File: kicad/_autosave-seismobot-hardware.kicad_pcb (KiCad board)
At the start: 4 copper layers, 110 x 111 mm, 98 parts, among them J1 Screw_Terminal_01x02, J2 Raspberry_Pi_2_3, U1 OPA2156xD, U10 AP7340, U2 OPA2156xD, U3 ref-6, U4 ref-8, U5 LTC6011, U6 OPA2156xD, U7 OPA2156xD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

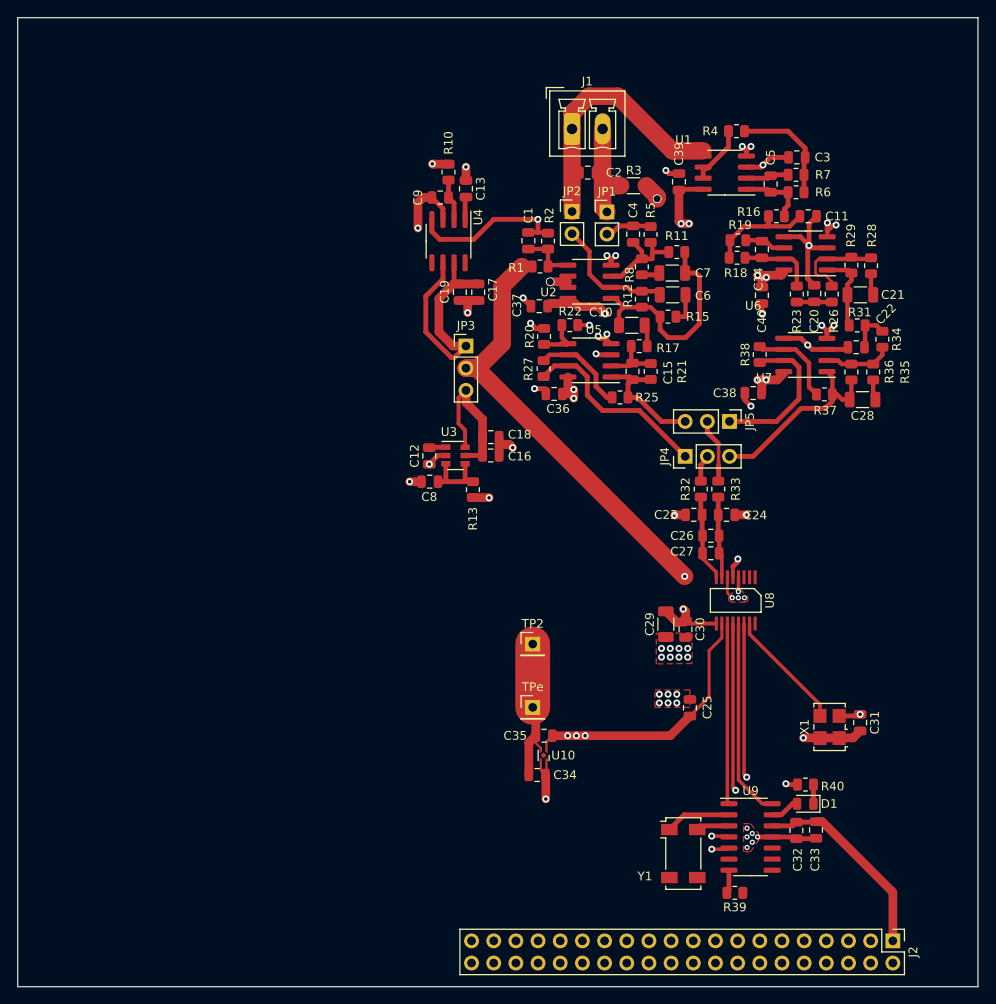
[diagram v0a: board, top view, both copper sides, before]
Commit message: add 3v3 regulator, more routing
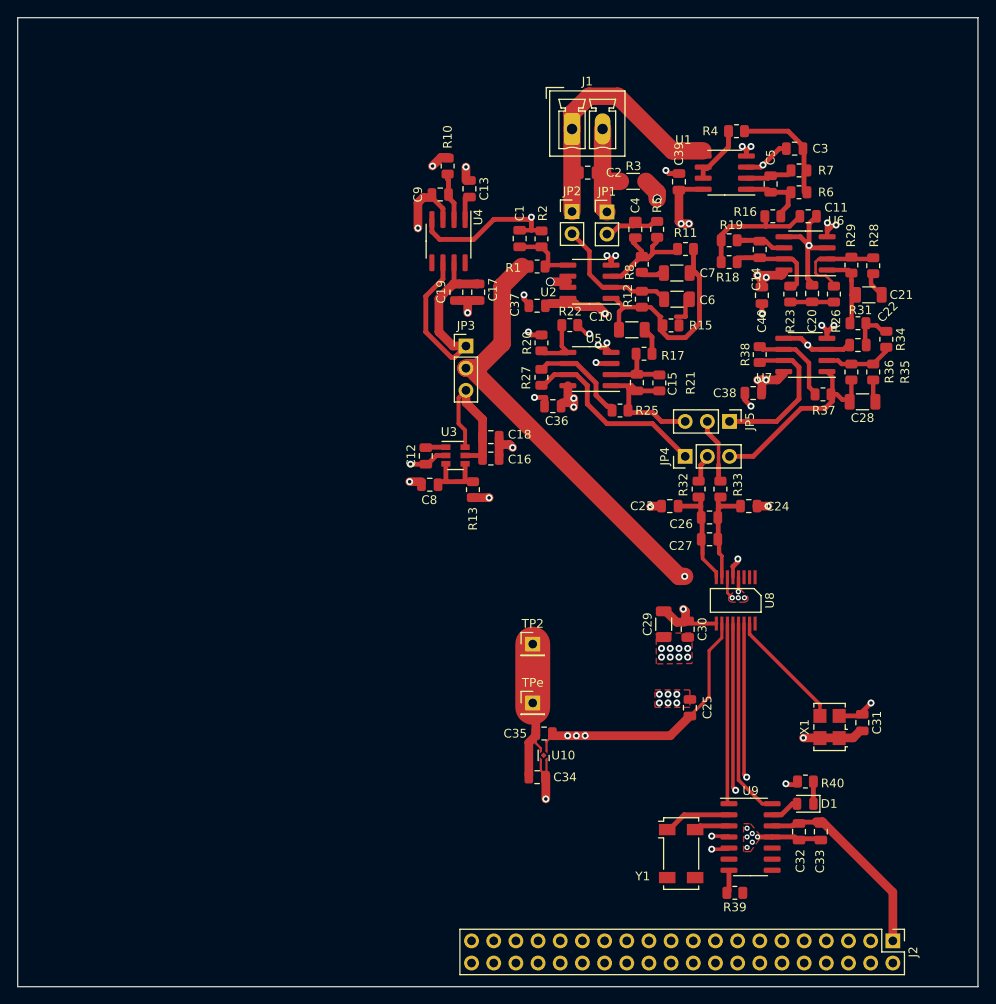
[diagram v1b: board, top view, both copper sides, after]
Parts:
- moved C23 2.93 mm to (133.7, 139.9)
- moved C24 2.74 mm to (142.8, 139.9)
- moved C26 2.11 mm to (138.2, 141.2)
- moved R21 1.64 mm to (132.5, 125.8)
- moved C27 1.61 mm to (138.2, 143.8)
- moved R25 1.50 mm to (128.0, 129.0)
- moved C36 1.41 mm to (120.3, 128.5)
- moved C15 1.38 mm to (129.9, 125.8)
- moved R11 1.06 mm to (135.5, 110.5)
- moved R15 1.06 mm to (133.8, 119.2)
- moved R18 1.04 mm to (140.5, 112.0)
- moved R17 1.03 mm to (130.8, 122.5)
- moved C1 1.03 mm to (116.5, 109.3)
- moved C3 1.03 mm to (148.0, 99.0)
- moved R27 1.03 mm to (119.0, 125.2)
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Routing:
- net GND: track 96.5 -> 101.5 mm
- net Net-(C14-Pad1): track 4.72 -> 8.35 mm
- net Net-(C14-Pad2): track 8.80 -> 12.0 mm
- net Net-(C24-Pad2): track 9.44 -> 12.1 mm
- net Net-(C23-Pad1): track 10.3 -> 12.9 mm
- net Net-(C4-Pad1): track 5.42 -> 7.01 mm
- net Net-(C15-Pad1): track 6.69 -> 8.24 mm
- net OUTa-: track 14.6 -> 16.0 mm
- net Net-(C4-Pad2): track 12.7 -> 14.0 mm
- net Net-(C11-Pad2): track 12.5 -> 13.7 mm
- net +3V3: track 109.5 -> 110.7 mm
- net 1.5v: track 106.1 -> 107.1 mm
- net Net-(R20-Pad1): track 5.18 -> 6.18 mm
- net Net-(C20-Pad2): track 4.00 -> 4.75 mm
- net Net-(C9-Pad2): track 4.79 -> 5.52 mm
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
